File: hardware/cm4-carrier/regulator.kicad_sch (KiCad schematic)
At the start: 9 parts, among them U2 TPS61088

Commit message: Fix four footprint identifiers not found in KiCad libraries
"Update PCB from Schematic" reported four footprints missing; correct them to
the actual names in the current KiCad libraries (edited in place to preserve
symbol UUIDs, so existing PCB associations are kept):

- J1 USB-C: USB_C_Receptacle_GCT_USB4110-GF-A_16P_TopMnt_Horizontal
            -> USB_C_Receptacle_GCT_USB4110
- L1 inductor: L_Bourns-SRP1265A -> L_Bourns_SRP1245A (SRP1265A not in KiCad;
  pick the footprint matching your actual boost inductor)
- U1 BQ24075: VQFN-16-1EP_3x3mm_P0.5mm_EP1.7x1.7mm
            -> QFN-16-1EP_3x3mm_P0.5mm_EP1.7x1.7mm
- U3 MAX17048: DFN-8-1EP_2x2mm_P0.5mm_EP0.61x1.42mm
            -> DFN-8-1EP_2x2mm_P0.5mm_EP0.9x1.5mm

README BOM updated to match.

Co-Authored-By: Claude Opus 4.8 <noreply@anthropic.com>
Claude-Session: https://claude.ai/code/session_015B7X7FE461jFSRaiTFdnFt
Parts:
- L1: footprint Inductor_SMD:L_Bourns-SRP1265A -> Inductor_SMD:L_Bourns_SRP1245A
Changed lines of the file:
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@@
 		(property "Value" "1uH" (at 90.00 100.08 0)
 			(effects (font (size 1.27 1.27)) (justify left)))
-		(property "Footprint" "Inductor_SMD:L_Bourns-SRP1265A" (at 90.00 95.00 90)
+		(property "Footprint" "Inductor_SMD:L_Bourns_SRP1245A" (at 90.00 95.00 90)
 			(effects (font (size 1.27 1.27)) (hide yes)))
 		(property "Datasheet" "" (at 90.00 95.00 0)

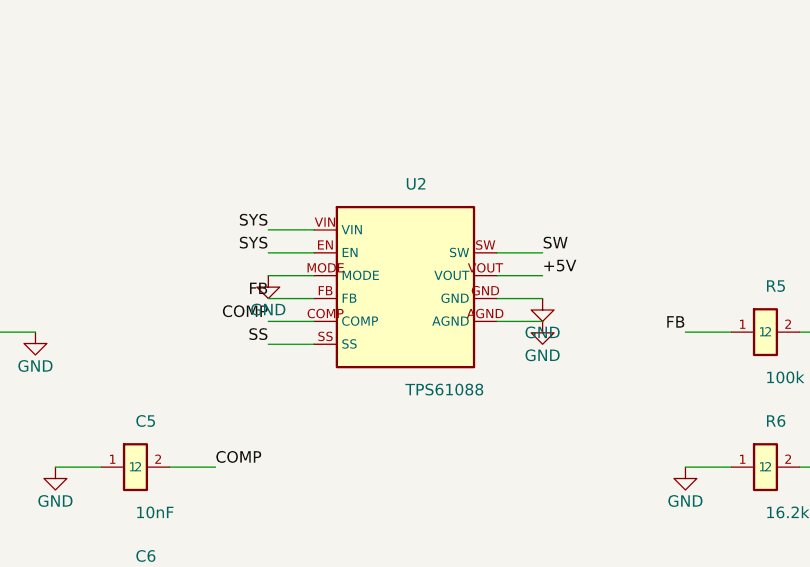
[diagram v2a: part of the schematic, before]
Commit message: hardware: remap U2 (TPS61088) to real 20-pin pinout + document errata
The TPS61088 symbol used pin numbers that were signal names, so Update PCB
from Schematic failed with "pad not found" for all ten pins. Remapped to the
datasheet RHL pinout (VCC=1, EN=2, FSW=3, SW=4-7, BOOT=8, VIN=9, SS=10,
NC=11/12, MODE=13, VOUT=14-16, FB=17, COMP=18, ILIM=19, AGND=20, PGND=EP/21),
verified against two independent community symbols.

- Paralleled SW (4-7) and VOUT (14-16) pads are stacked onto their nets so
  every high-current pad is connected.
- The previously absent VCC/FSW/BOOT/ILIM pins are added (unwired) so ERC
  flags the support network that still must be added before fab; NC pads
  11/12 marked no-connect. FSW/ILIM resistor values are intentionally left to
  the datasheet rather than guessed.

README: new "Errata - symbol pad mapping" section documenting the J1/U3/U2
fixes and the outstanding TPS61088 support network.

Co-Authored-By: Claude Opus 4.8 <noreply@anthropic.com>
Claude-Session: https://claude.ai/code/session_019TySzotXwMtpz6QGTRfF9s
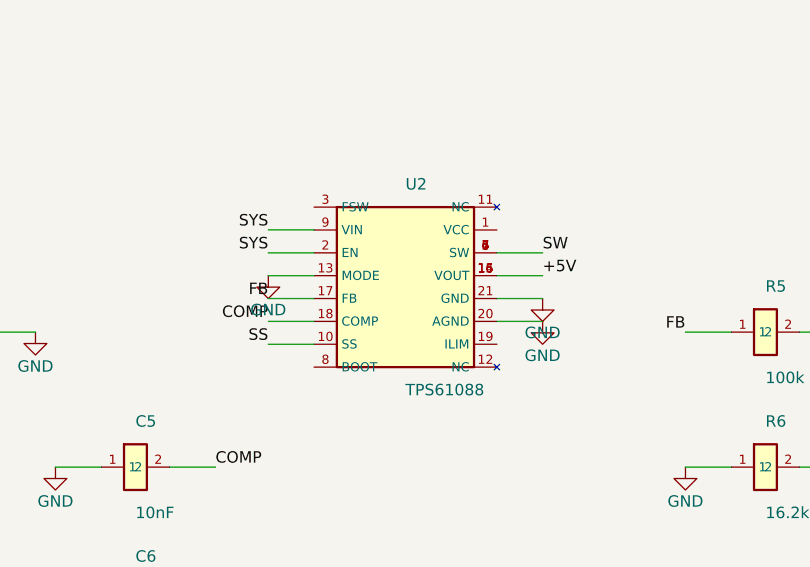
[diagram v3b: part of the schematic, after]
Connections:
- net +5V: now also U2.14 (VOUT), U2.15 (VOUT), U2.16 (VOUT); no longer U2.VOUT
- net COMP: now also U2.18 (COMP); no longer U2.COMP
- net FB: now also U2.17 (FB); no longer U2.FB
- net GND: now also U2.13 (MODE), U2.20 (AGND), U2.21 (GND); no longer U2.AGND, U2.GND, U2.MODE
- net SS: now also U2.10 (SS); no longer U2.SS
- net SW: now also U2.4 (SW), U2.5 (SW), U2.6 (SW), U2.7 (SW); no longer U2.SW
- net SYS: now also U2.2 (EN), U2.9 (VIN); no longer U2.EN, U2.VIN
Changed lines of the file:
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@@
 		(property "Datasheet" "https://www.ti.com/lit/ds/symlink/tps61088.pdf" (at 90.00 55.00 0)
 			(effects (font (size 1.27 1.27)) (hide yes)))
-		(pin "VIN")
-		(pin "EN")
-		(pin "MODE")
-		(pin "FB")
-		(pin "COMP")
-		(pin "SS")
-		(pin "SW")
-		(pin "VOUT")
-		(pin "GND")
-		(pin "AGND")
+		(pin "9")
+		(pin "2")
+		(pin "13")
+		(pin "17")
+		(pin "18")
+		(pin "10")
+		(pin "4")
+		(pin "14")
+		(pin "21")
+		(pin "20")
+		(pin "5")
+		(pin "6")
+		(pin "7")
+		(pin "15")
+		(pin "16")
+		(pin "1")
+		(pin "3")
+		(pin "8")
+		(pin "19")
+		(pin "11")
+		(pin "12")
 		(instances
 			(project "cm4-carrier"
